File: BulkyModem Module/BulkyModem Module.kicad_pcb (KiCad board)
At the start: 2 copper layers, 100 x 100 mm, 94 parts, among them J1 DC IN, J2 DCE, J3 Module_Panel, J4 Conn_Power, J5 C64_Modem_IDC, K1 HK19F-DC, M1 Mounting, M2 Mounting, M3 Mounting, M4 Mounting, Q1 2N3904, Q2 2N3904, Q3 2N3904, Q4 2N3904, Q5 2N3904, Q6 2N3904, Q7 2N3904, Q8 2N3904, U1 74HCT244, U2 74HCT04, U3 MAX232, U4 MAX232

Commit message: Initial layout
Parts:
- removed Q2, Q3: 2N3904, Package_TO_SOT_THT:TO-92_Inline_Wide
- removed R3: 4k7, resistor:R_Axial_DIN0207_L6.3mm_D2.5mm_P10.16mm_Horizontal
- removed R5: 10k, resistor:R_Axial_DIN0207_L6.3mm_D2.5mm_P10.16mm_Horizontal
- removed R6: 470, resistor:R_Axial_DIN0207_L6.3mm_D2.5mm_P10.16mm_Horizontal
- added C19: 100nF, Capacitor_THT:C_Disc_D4.7mm_W2.5mm_P5.00mm, F.Cu at (138.4, 83.2)
- added C20: 22uF, Capacitor_THT:CP_Radial_D5.0mm_P2.00mm, F.Cu at (152.4, 127.6)
- added JP14: INV_RI, Jumper:SolderJumper-3_P1.3mm_Open_RoundedPad1.0x1.5mm, F.Cu at (151.1, 117.5)
- added U5: 74HCT04, Package_DIP:DIP-14_W7.62mm_Socket_LongPads, F.Cu at (149.9, 114.3)
- C7: value 22uF -> 100nF; footprint Capacitor_THT:CP_Radial_D5.0mm_P2.00mm -> Capacitor_THT:C_Disc_D4.7mm_W2.5mm_P5.00mm
- D3: value DATA -> RI
- J5: footprint BulkyModem:C64_Adapter_IDC -> BulkyModem:UserPort_Adapter_IDC
- JP13: value NO_DCD -> BYPASS
- R2: value 10k -> 470
- moved Q1 234.8 mm to (159.4, 125.1), turned to 270 degrees
- moved R18 227.2 mm to (165.1, 66.7), turned to 180 degrees
- moved U1 220.1 mm to (142.2, 89.5), turned to 90 degrees
- moved R2 219.1 mm to (151.1, 135.9)
- moved R16 215.4 mm to (148.0, 125.1), turned to 270 degrees
- moved R11 213.0 mm to (118.1, 132.7)
- moved R1 205.4 mm to (151.1, 132.7)
- moved Q7 205.4 mm to (113.7, 125.1), turned to 270 degrees
- moved R22 203.0 mm to (157.5, 93.3), turned to 180 degrees
- moved R23 202.2 mm to (133.3, 93.3)
- moved R15 198.7 mm to (144.1, 125.1), turned to 270 degrees
- moved R21 196.6 mm to (116.8, 118.1), turned to 90 degrees
- moved Q6 194.0 mm to (126.4, 125.1), turned to 270 degrees
- moved R17 191.2 mm to (133.3, 81.9), turned to 180 degrees
- moved R20 188.8 mm to (141.0, 66.7)
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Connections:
- A1 pad 23: Net-(A1-Pad23) -> ESP_RI
- C7 pad 1: Net-(C7-Pad1) -> +5V
- D3 pad 1: /Front panel/LED_DATA -> /Front panel/LED_RI
- J2 pad 9: (no net) -> /RS-232/SER_RI
- J3 pad 10: /Front panel/LED_RS232 -> /Front panel/LED_RI
- J3 pad 11: /Front panel/LED_C64 -> /Front panel/LED_RS232
- J3 pad 12: (no net) -> /Front panel/LED_C64
- J3 pad 4: /Front panel/LED_DATA -> (no net)
- J5 pad 10: ESP_DCD -> GND
- J5 pad 6: GND -> ESP_DCD
- J5 pad 7: GND -> ESP_RI
- J5 pad 8: GND -> (no net)
- Q1 pad 1: Net-(Q1-Pad1) -> GND
- Q1 pad 3: +5V -> Net-(C20-Pad1)
- R1 pad 1: Net-(Q2-Pad2) -> Net-(Q1-Pad2)
- R1 pad 2: ESP_TX -> ESP_RI
- R2 pad 1: Net-(Q1-Pad2) -> Net-(C20-Pad1)
- R2 pad 2: ESP_RX -> /Front panel/LED_RI
- U4 pad 10: GND -> Net-(JP14-Pad2)
- U4 pad 7: (no net) -> /RS-232/SER_RI
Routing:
- net +5V: track 211.9 -> 588.8 mm, vias 0 -> 2
- net ESP_TX: track 5.08 -> 195.2 mm, vias 0 -> 3
- net ESP_RTS: track 5.08 -> 181.8 mm, vias 0 -> 3
- net ESP_RX: track 0.00 -> 174.8 mm, vias 0 -> 4
- net ESP_CTS: track 0.00 -> 152.1 mm, vias 0 -> 4
- net ESP_RI: track 0.00 -> 133.5 mm, vias 0 -> 1
- net /RS-232/DCE_CTS: track 0.00 -> 99.6 mm
- net MODE_232: track 0.00 -> 98.1 mm, vias 0 -> 1
- net ESP_DCD: track 5.08 -> 102.6 mm, vias 0 -> 3
- net MODE_C64: track 0.00 -> 87.1 mm, vias 0 -> 4
- net Net-(JP14-Pad2): track 0.00 -> 82.9 mm, vias 0 -> 2
- net /RS-232/DCE_RTS: track 0.00 -> 68.5 mm, vias 0 -> 1
- net Net-(JP11-Pad3): track 0.00 -> 65.5 mm, vias 0 -> 2
- net /Front panel/LED_RI: track 0.00 -> 65.1 mm, vias 0 -> 2
- net Net-(JP12-Pad2): track 0.00 -> 54.5 mm, vias 0 -> 1
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
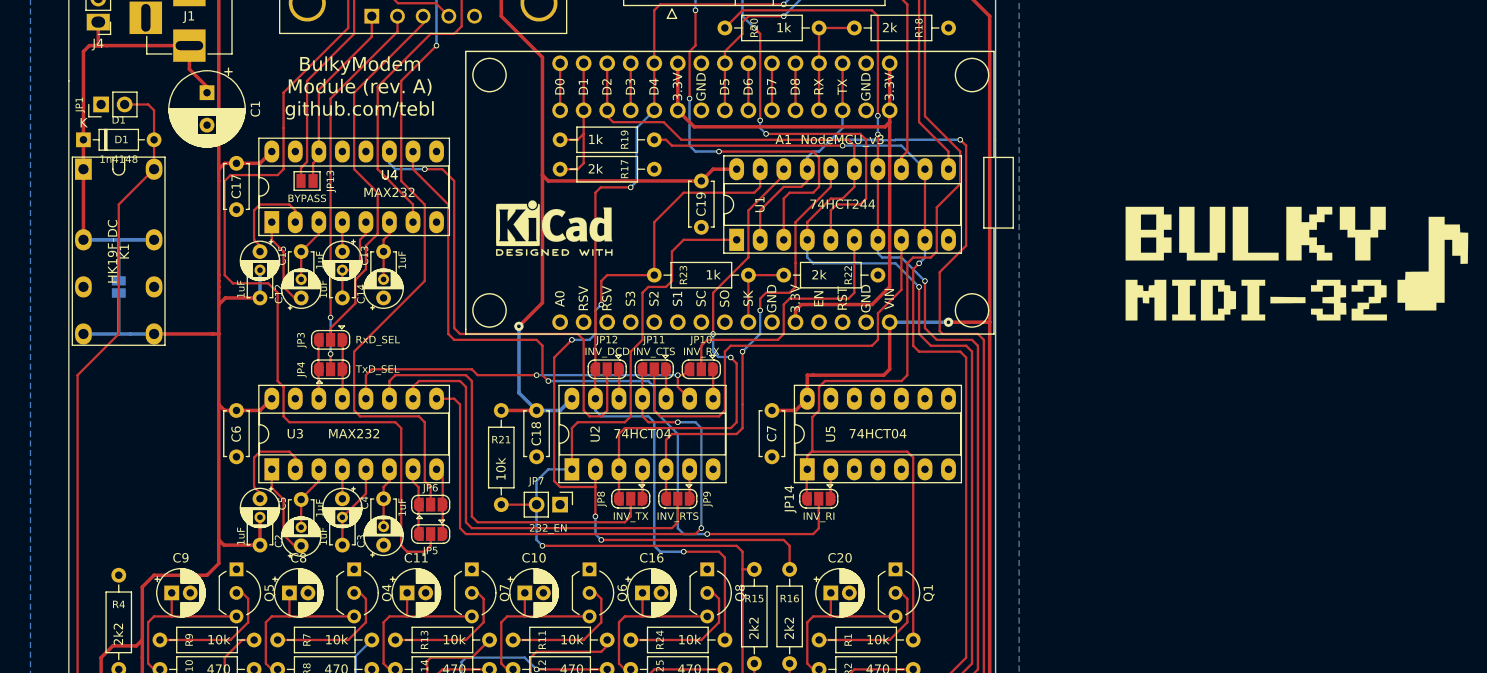
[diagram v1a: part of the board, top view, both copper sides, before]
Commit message: Silkscreen tweaks
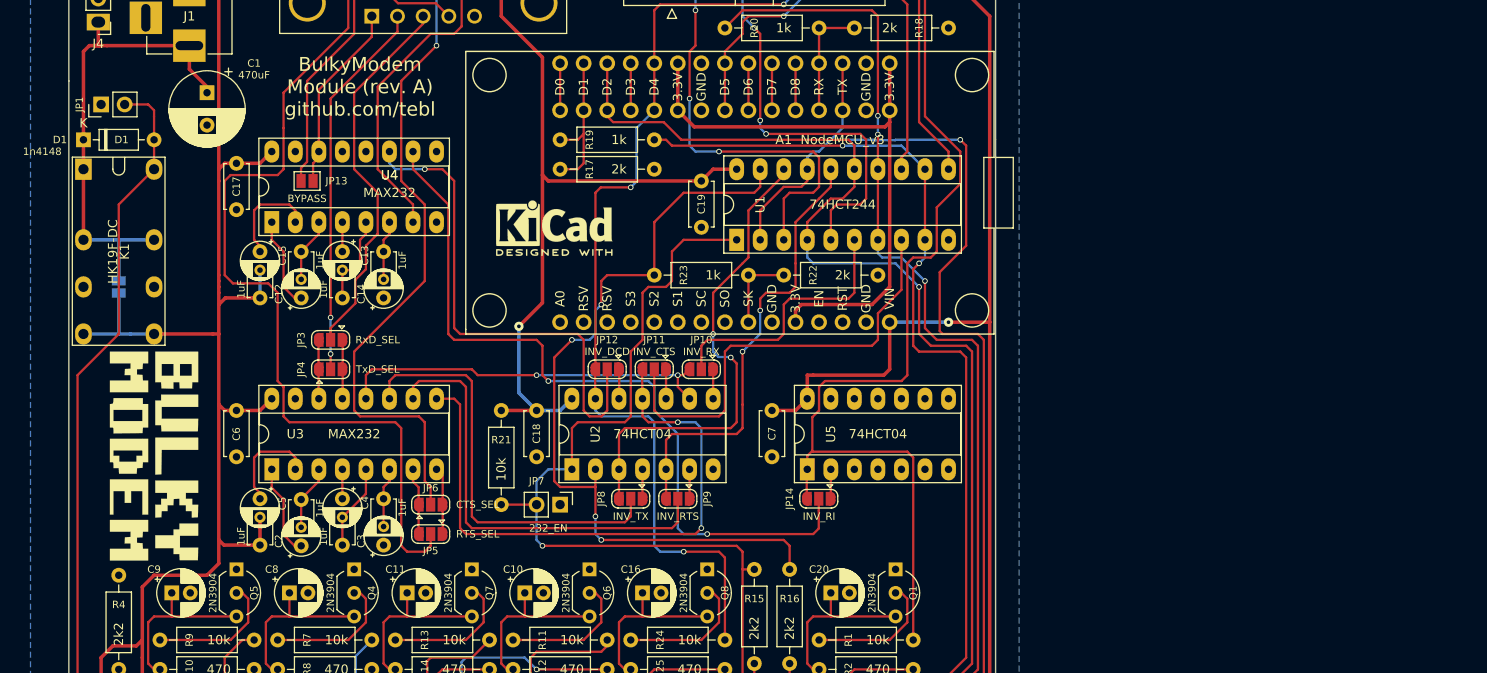
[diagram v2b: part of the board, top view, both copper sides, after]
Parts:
- G*** (x2): footprint artwork:BulkyMIDI-32_8bit -> artwork:BulkyModem
- moved G*** 125.6 mm to (79.4, 113.0), turned to 270 degrees
- moved G*** 125.2 mm to (79.4, 112.4), turned to 90 degrees

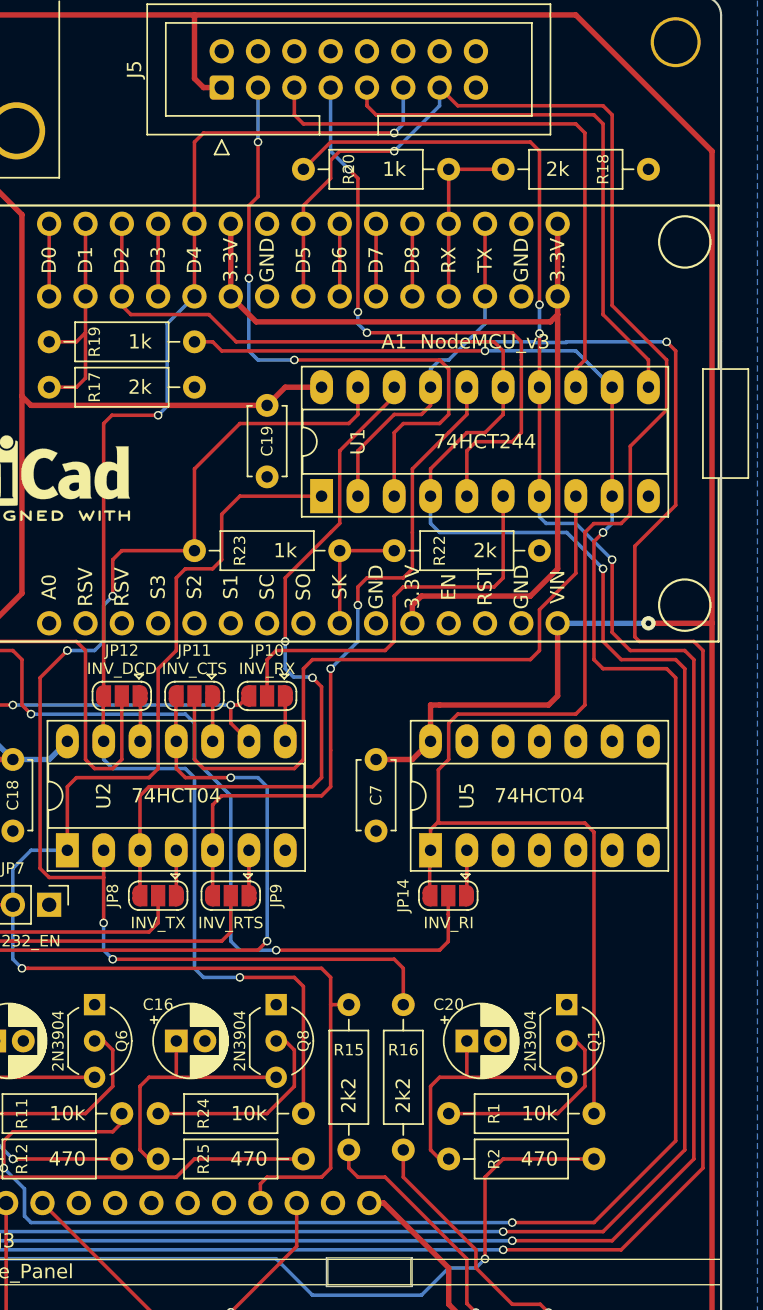
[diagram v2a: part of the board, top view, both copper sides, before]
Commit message: Buffer RI and DCD with spare gates
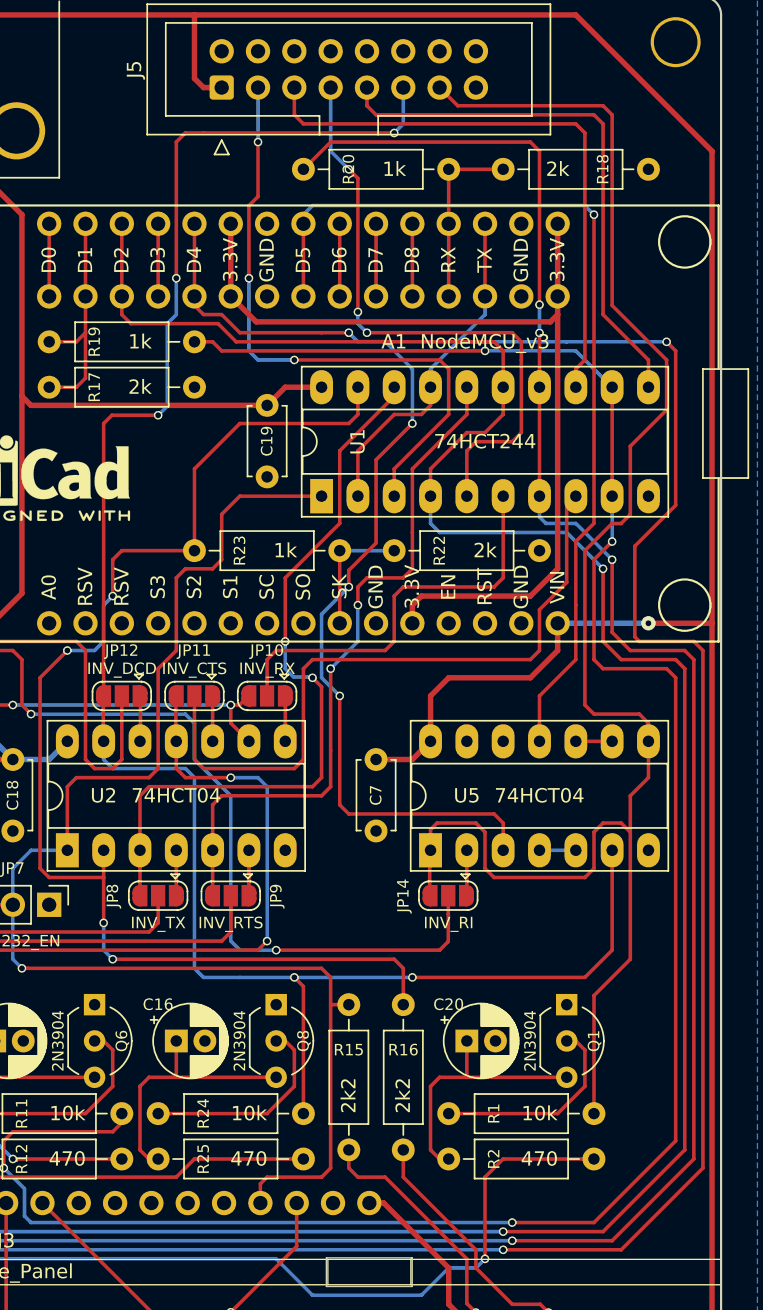
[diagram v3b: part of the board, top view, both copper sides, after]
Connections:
- A1 pad 23: ESP_RI -> Net-(A1-Pad23)
- A1 pad 26: ESP_DCD -> Net-(A1-Pad26)
- U5 pad 10: (no net) -> Net-(U5-Pad10)
- U5 pad 11: GND -> Net-(A1-Pad23)
- U5 pad 3: GND -> Net-(A1-Pad26)
- U5 pad 4: (no net) -> Net-(U5-Pad4)
- U5 pad 5: GND -> Net-(U5-Pad4)
- U5 pad 6: (no net) -> ESP_DCD
- U5 pad 8: (no net) -> ESP_RI
- U5 pad 9: GND -> Net-(U5-Pad10)
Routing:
- net Net-(A1-Pad26): track 0.00 -> 70.3 mm, vias 0 -> 4
- net Net-(A1-Pad23): track 0.00 -> 65.0 mm, vias 0 -> 1
- net ESP_DCD: track 102.6 -> 133.4 mm, vias 3 -> 5
- net ESP_RI: track 133.5 -> 117.5 mm, vias 1 -> 0
- net Net-(U5-Pad4): track 0.00 -> 2.54 mm
- net Net-(U5-Pad10): track 0.00 -> 2.54 mm
- net /C64_TX: track 45.1 -> 43.6 mm
- net +5V: track 588.8 -> 587.3 mm
